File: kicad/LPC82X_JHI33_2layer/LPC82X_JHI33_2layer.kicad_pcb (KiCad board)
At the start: 2 copper layers, 26 x 23.5 mm, 27 parts, among them J1 Conn_02x09_Odd_Even, J2 Conn_02x09_Odd_Even, J3 JTAG_2X05, U1 LPC824M201JHI33, Y1 12MHz

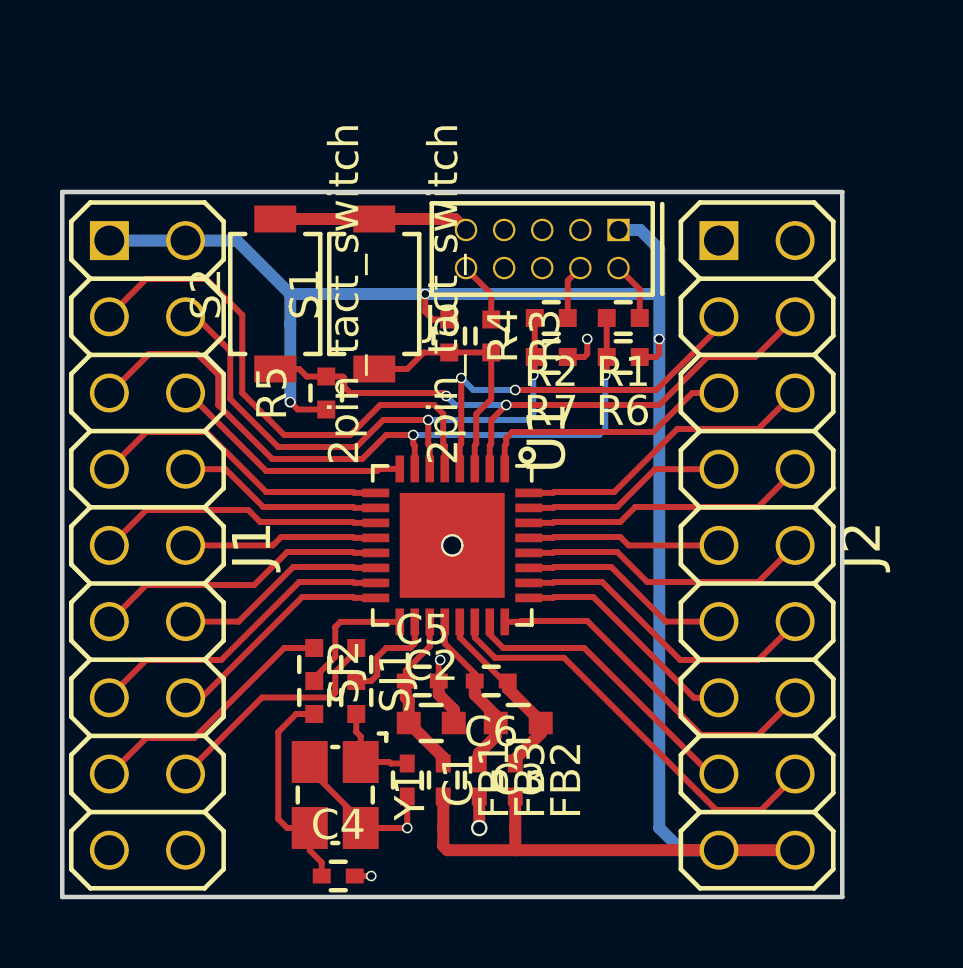
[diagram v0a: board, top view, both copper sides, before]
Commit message: added bulk decoupling 0805 increased clearance of ground plane
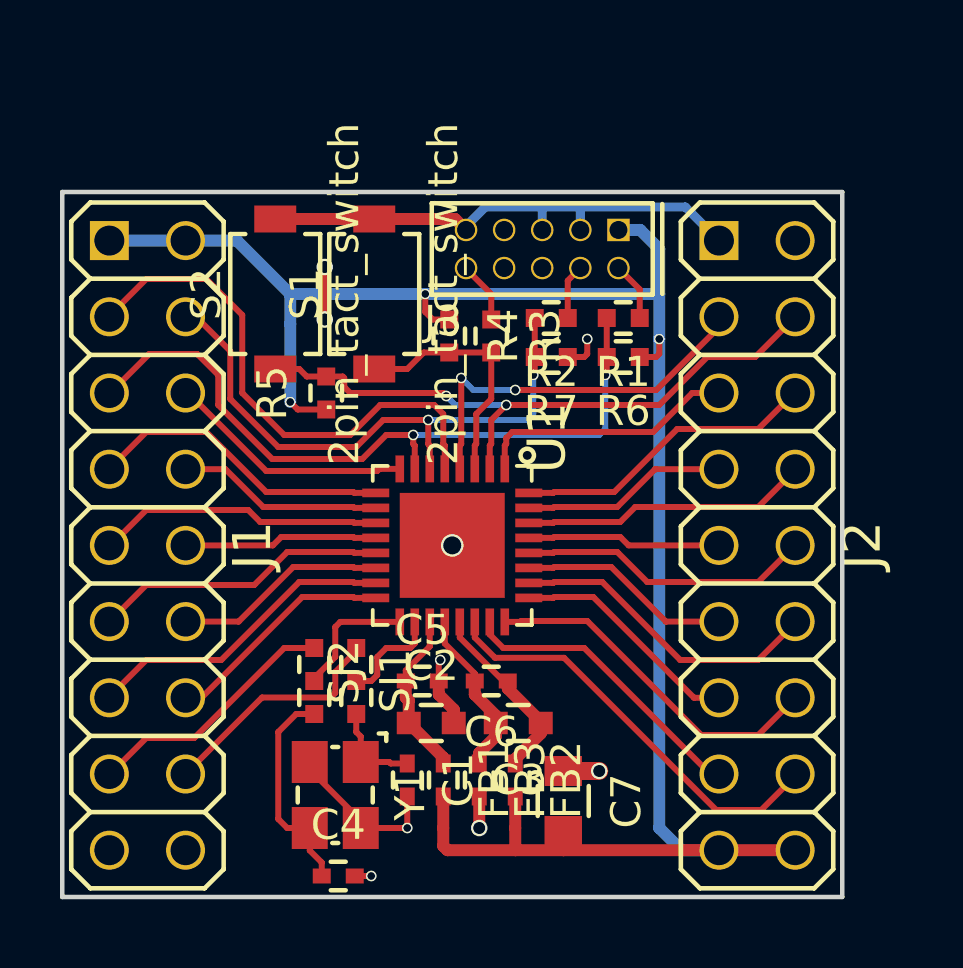
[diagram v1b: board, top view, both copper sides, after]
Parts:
- added C7: 10u, SquantorRcl:C_0805, F.Cu at (92.6, 115.2)
- FB1, FB2, FB3: value Ferrite_Bead_Small -> FB
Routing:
- net VSS: track 17.1 -> 31.1 mm, vias 6 -> 9
- net VDD: track 65.1 -> 65.8 mm
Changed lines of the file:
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@@
     (thickness 1.6)
     (drawings 4)
-    (tracks 351)
+    (tracks 368)
     (zones 0)
-    (modules 27)
+    (modules 28)
     (nets 42)
   )
@@
   )
   (setup
-    (last_trace_width 0.2)
+    (last_trace_width 0.3)
     (user_trace_width 0.127)
     (user_trace_width 0.2)
@@
     (user_trace_width 2)
     (trace_clearance 0.127)
-    (zone_clearance 0.2)
+    (zone_clearance 0.3)
     (zone_45_only no)
     (trace_min 0.127)
@@
       (effects (font (size 1 1) (thickness 0.15)))
     )
-    (fp_text value Ferrite_Bead_Small (at 0 1.7) (layer F.Fab)
+    (fp_text value FB (at 0 1.7) (layer F.Fab)
       (effects (font (size 1 1) (thickness 0.15)))
     )
@@
       (effects (font (size 1 1) (thickness 0.15)))
     )
-    (fp_text value Ferrite_Bead_Small (at 0 1.7 270) (layer F.Fab)
+    (fp_text value FB (at 0 1.7 270) (layer F.Fab)
       (effects (font (size 1 1) (thickness 0.15)))
     )
@@
       (effects (font (size 1 1) (thickness 0.15)))
     )
-    (fp_text value Ferrite_Bead_Small (at 0 1.7 270) (layer F.Fab)
+    (fp_text value FB (at 0 1.7 270) (layer F.Fab)
       (effects (font (size 1 1) (thickness 0.15)))
     )
@@
     )
   )
+  (module SquantorRcl:C_0805 (layer F.Cu)
+    (at 92.6 115.2 270)
+    (descr "Capacitor SMD 0805, reflow soldering, AVX (see smccp.pdf)")
+    (tags "capacitor 0805")
+    (attr smd)
+    (fp_text reference C7 (at 0 -2.1 270) (layer F.SilkS)
+      (effects (font (size 1 1) (thickness 0.15)))
+    )
+    (fp_text value 10u (at 0 2.1 270) (layer F.Fab)
+      (effects (font (size 1 1) (thickness 0.15)))
+    )
+    (fp_line (start -1 0.625) (end -1 -0.625) (layer F.Fab) (width 0.15))
+    (fp_line (start 1 0.625) (end -1 0.625) (layer F.Fab) (width 0.15))
+    (fp_line (start 1 -0.625) (end 1 0.625) (layer F.Fab) (width 0.15))
+    (fp_line (start -1 -0.625) (end 1 -0.625) (layer F.Fab) (width 0.15))
+    (fp_line (start -1.8 -1) (end 1.8 -1) (layer F.CrtYd) (width 0.05))
+    (fp_line (start -1.8 1) (end 1.8 1) (layer F.CrtYd) (width 0.05))
+    (fp_line (start -1.8 -1) (end -1.8 1) (layer F.CrtYd) (width 0.05))
+    (fp_line (start 1.8 -1) (end 1.8 1) (layer F.CrtYd) (width 0.05))
+    (fp_line (start 0.5 -0.85) (end -0.5 -0.85) (layer F.SilkS) (width 0.15))
+    (fp_line (start -0.5 0.85) (end 0.5 0.85) (layer F.SilkS) (width 0.15))
+    (pad 1 smd rect (at -1 0 270) (size 1 1.25) (layers F.Cu F.Paste F.Mask)
+      (net 2 VSS))
+    (pad 2 smd rect (at 1 0 270) (size 1 1.25) (layers F.Cu F.Paste F.Mask)
+      (net 7 VDD))
+    (model Capacitors_SMD.3dshapes/C_0805.wrl
+      (at (xyz 0 0 0))
+      (scale (xyz 1 1 1))
+      (rotate (xyz 0 0 0))
+    )
+  )
   (gr_line (start 75.9 118.4) (end 75.9 94.9) (layer Edge.Cuts) (width 0.15))
   (gr_line (start 101.9 118.4) (end 75.9 118.4) (layer Edge.Cuts) (width 0.15))
   (gr_line (start 101.9 94.9) (end 101.9 118.4) (layer Edge.Cuts) (width 0.15))
   (gr_line (start 75.9 94.9) (end 101.9 94.9) (layer Edge.Cuts) (width 0.15))
+  (via (at 84.65 99.15) (size 0.55) (drill 0.4) (layers F.Cu B.Cu) (net 2))
+  (segment (start 84.65 99.15) (end 84.65 97.4) (width 0.3) (layer F.Cu) (net 2))
+  (via (at 84.65 97.4) (size 0.55) (drill 0.4) (layers F.Cu B.Cu) (net 2))
   (segment (start 85.7 112.3) (end 85.7 112.9) (width 0.2) (layer F.Cu) (net 1))
   (segment (start 85.85 113.05) (end 85.85 113.9) (width 0.2) (layer F.Cu) (net 1))
@@
   (segment (start 88.995 95.8) (end 89.36 96.165) (width 0.4) (layer F.Cu) (net 2))
   (segment (start 86.3 95.8) (end 88.995 95.8) (width 0.4) (layer F.Cu) (net 2))
+  (segment (start 92.6 114.2) (end 93.8 114.2) (width 0.6) (layer F.Cu) (net 2))
+  (via (at 93.8 114.2) (size 0.55) (drill 0.4) (layers F.Cu B.Cu) (net 2))
+  (segment (start 89.36 96.165) (end 89.36 96.04) (width 0.3) (layer F.Cu) (net 2))
+  (segment (start 89.36 96.165) (end 89.36 96.04) (width 0.3) (layer B.Cu) (net 2))
+  (segment (start 89.36 96.04) (end 90 95.4) (width 0.3) (layer B.Cu) (net 2))
+  (segment (start 91.9 96.165) (end 91.9 95.4) (width 0.3) (layer B.Cu) (net 2))
+  (segment (start 90 95.4) (end 91.9 95.4) (width 0.3) (layer B.Cu) (net 2))
+  (segment (start 96.67 95.4) (end 97.79 96.52) (width 0.3) (layer B.Cu) (net 2))
+  (segment (start 93.17 95.48) (end 93.25 95.4) (width 0.3) (layer B.Cu) (net 2))
+  (segment (start 93.17 96.165) (end 93.17 95.48) (width 0.3) (layer B.Cu) (net 2))
+  (segment (start 91.9 95.4) (end 93.25 95.4) (width 0.3) (layer B.Cu) (net 2))
+  (segment (start 93.25 95.4) (end 96.67 95.4) (width 0.3) (layer B.Cu) (net 2))
   (segment (start 87.35 111.2) (end 87.35 110.85) (width 0.2) (layer F.Cu) (net 3))
   (segment (start 88.15 110.05) (end 88.15 109.23) (width 0.2) (layer F.Cu) (net 3))
@@
   (segment (start 88.74 116.84) (end 88.6 116.7) (width 0.4) (layer F.Cu) (net 7))
   (segment (start 91 116.1) (end 91 116.84) (width 0.4) (layer F.Cu) (net 7))
-  (segment (start 97.79 116.84) (end 91 116.84) (width 0.4) (layer F.Cu) (net 7))
   (segment (start 91 116.84) (end 88.74 116.84) (width 0.4) (layer F.Cu) (net 7))
   (segment (start 77.47 96.52) (end 80.01 96.52) (width 0.4) (layer B.Cu) (net 7))
@@
   (segment (start 83.5 98.3) (end 88 98.3) (width 0.4) (layer B.Cu) (net 7))
   (segment (start 88 98.3) (end 95.8 98.3) (width 0.4) (layer B.Cu) (net 7))
+  (segment (start 92.6 116.2) (end 92.6 116.84) (width 0.4) (layer F.Cu) (net 7))
+  (segment (start 97.79 116.84) (end 92.6 116.84) (width 0.4) (layer F.Cu) (net 7))
+  (segment (start 92.6 116.84) (end 91 116.84) (width 0.4) (layer F.Cu) (net 7))
   (segment (start 77.47 99.06) (end 77.47 99.03) (width 0.2) (layer B.Cu) (net 8))
   (segment (start 88.65 103.35) (end 88.65 104.13) (width 0.2) (layer F.Cu) (net 8))
@@
   (segment (start 85.17 109.23) (end 85 109.4) (width 0.2) (layer F.Cu) (net 41))
   (zone (net 2) (net_name VSS) (layer B.Cu) (hatch edge 0.508)
-    (connect_pads (clearance 0.2))
-    (min_thickness 0.254)
+    (connect_pads (clearance 0.3))
+    (min_thickness 0.4)
     (fill yes (arc_segments 16) (thermal_gap 0.508) (thermal_bridge_width 0.508))
     (polygon

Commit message: silk screen updates
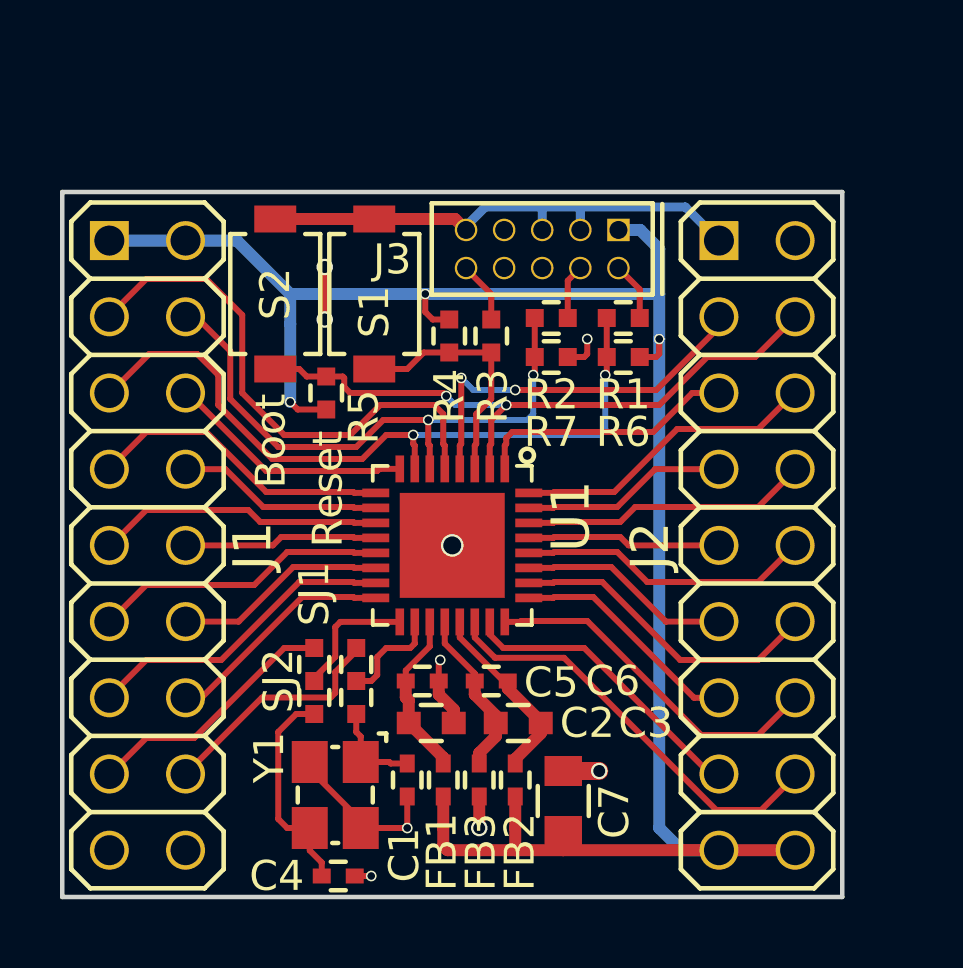
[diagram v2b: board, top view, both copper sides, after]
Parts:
- S1: value 2pin_tact_switch -> Reset
- S2: value 2pin_tact_switch -> Boot
- moved N2 9.19 mm to (84.2, 110.5)
- moved N1 9.12 mm to (85.0, 106.8)

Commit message: updated versionnumber
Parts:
- N2: value 20181026 -> 20181028
- moved N2 8.81 mm to (92.6, 108.0), turned to 270 degrees
- moved N1 3.70 mm to (88.7, 106.7), turned to 270 degrees
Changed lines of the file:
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@@
   )
   (module Symbols:OSHW-Symbol_6.7x6mm_SilkScreen (layer B.Cu)
-    (at 85 106.8 180)
+    (at 88.7 106.7 270)
     (descr "Open Source Hardware Symbol")
     (tags "Logo Symbol OSHW")
     (attr virtual)
-    (fp_text reference N1 (at 0 0 180) (layer B.SilkS) hide
+    (fp_text reference N1 (at 0 0 270) (layer B.SilkS) hide
       (effects (font (size 1 1) (thickness 0.15)) (justify mirror))
     )
-    (fp_text value OHWLOGO (at 0.75 0 180) (layer B.Fab) hide
+    (fp_text value OHWLOGO (at 0.75 0 270) (layer B.Fab) hide
       (effects (font (size 1 1) (thickness 0.15)) (justify mirror))
     )
@@
   )
   (module SquantorLabels:Label_version (layer B.Cu)
-    (at 84.15 110.45 180)
-    (fp_text reference N2 (at 0 -1.4 180) (layer B.Fab) hide
+    (at 92.6 107.95 270)
+    (fp_text reference N2 (at 0 -1.4 270) (layer B.Fab) hide
       (effects (font (size 1 1) (thickness 0.15)) (justify mirror))
     )
-    (fp_text value 20181026 (at -0.4 0.137362 180) (layer B.SilkS)
+    (fp_text value 20181028 (at -0.4 0.137362 270) (layer B.SilkS)
       (effects (font (size 1 1) (thickness 0.15)) (justify mirror))
     )
-    (fp_text user V: (at -4.9 0.1 180) (layer B.SilkS)
+    (fp_text user V: (at -4.9 0.1 270) (layer B.SilkS)
       (effects (font (size 1 1) (thickness 0.15)) (justify mirror))
     )

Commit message: updated schematic bits updated board and rerouted with some deletions, lets see if we can shrink the board a bit
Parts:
- removed R5: 47K, SquantorRcl:R_0402_hand
- removed S1: Reset, SquantorButtons:TD-85XU
- removed S2: Boot, SquantorButtons:TD-85XU
- removed SJ1, SJ2: SolderJumper_3way_1conn, SquantorSpecial:solder_jumper_3way_12conn
- N2: value 20181028 -> 20181029
- R4: value 47K -> 100K
- moved C1 5.10 mm to (84.9, 110.0), turned to 180 degrees
- moved C4 2.36 mm to (84.9, 115.3)
- moved Y1 2.30 mm to (84.9, 112.7)
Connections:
- C1 pad 1: /XTALIN -> /PIO0_9
- C4 pad 1: /XTALOUT -> /PIO0_8
- U1 pad 17: /PIO0_9-XTALOUT -> /PIO0_9
- U1 pad 18: /PIO0_8-XTALIN -> /PIO0_8
- Y1 pad 1: /XTALIN -> /PIO0_9
- Y1 pad 3: /XTALOUT -> /PIO0_8
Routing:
- net /PIO0_8: track 7.90 -> 17.1 mm
- net /PIO0_12: track 21.6 -> 13.2 mm, vias 2 -> 0
- net /XTALOUT: track 7.29 -> 0.00 mm
- net VSS: track 31.1 -> 24.7 mm, vias 9 -> 8
- net /PIO0_9: track 8.57 -> 14.3 mm
- net VDD: track 65.8 -> 60.8 mm, vias 3 -> 2
- net /PIO0_9-XTALOUT: track 4.31 -> 0.00 mm
- net /PIO0_8-XTALIN: track 3.54 -> 0.00 mm
- net /XTALIN: track 3.23 -> 0.00 mm
- net /RESET: track 8.24 -> 5.51 mm
- net /PIO0_4: track 13.0 -> 12.2 mm

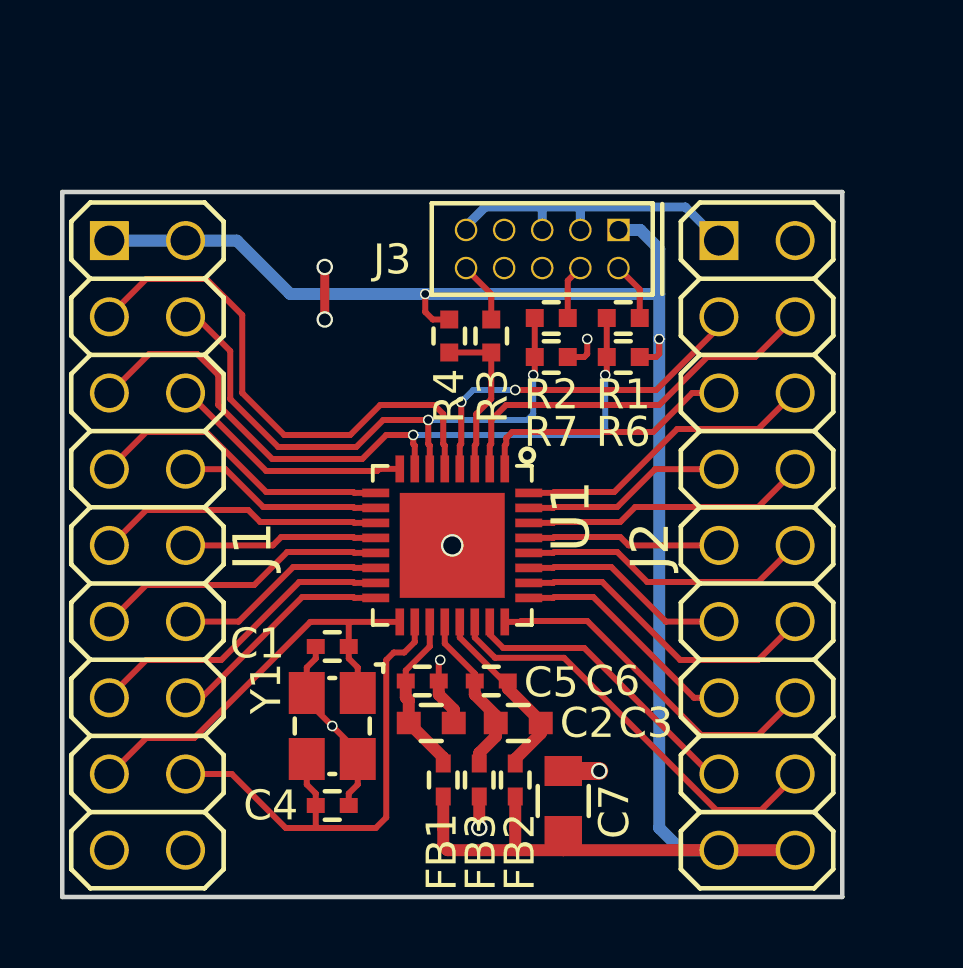
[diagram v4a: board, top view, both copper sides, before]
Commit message: reduced PCB size, rerouting large parts of it
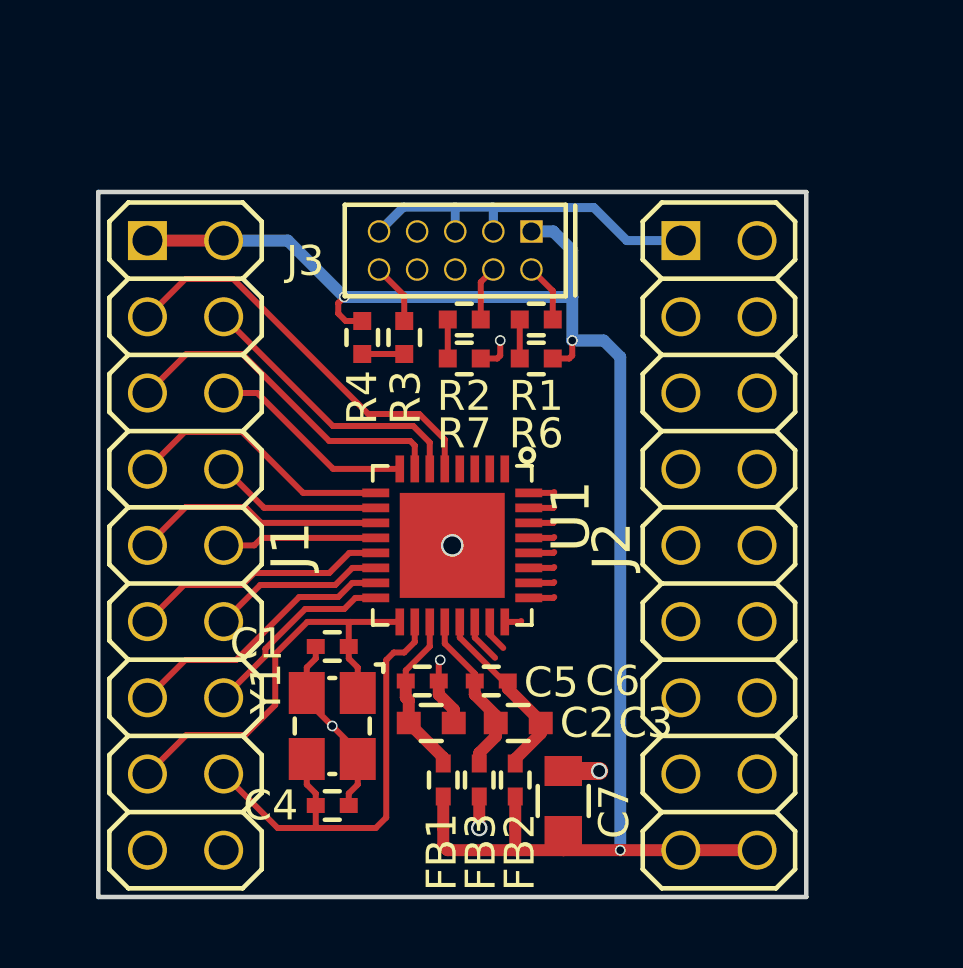
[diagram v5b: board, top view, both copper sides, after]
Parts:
- moved J3 2.90 mm to (89.0, 96.8)
- moved R2 2.90 mm to (89.3, 99.2)
- moved R3 2.90 mm to (87.3, 99.8)
- moved R7 2.90 mm to (89.3, 100.5)
- moved R1 2.90 mm to (91.7, 99.2)
- moved R4 2.90 mm to (85.9, 99.8)
- moved R6 2.90 mm to (91.7, 100.5)
- moved J1 1.27 mm to (80.0, 106.7)
- moved J2 1.27 mm to (97.8, 106.7)
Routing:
- net /PIO0_12: track 13.2 -> 0.00 mm
- net /PIO0_7: track 14.1 -> 1.48 mm
- net /PIO0_4: track 12.2 -> 0.00 mm, vias 2 -> 0
- net /PIO0_2: track 24.4 -> 12.8 mm, vias 2 -> 0
- net /PIO0_0: track 11.8 -> 0.56 mm
- net /PIO0_23: track 10.5 -> 0.86 mm
- net /PIO0_17: track 10.3 -> 0.86 mm
- net /PIO0_21: track 9.81 -> 0.86 mm
- net /PIO0_6: track 9.99 -> 1.06 mm
- net /PIO0_3: track 19.7 -> 10.8 mm, vias 2 -> 0
- net /PIO0_19: track 9.64 -> 0.86 mm
- net /PIO0_13: track 8.76 -> 0.00 mm
- net /PIO0_14: track 7.74 -> 0.86 mm
- net /PIO0_22: track 7.11 -> 0.86 mm
- net /PIO0_18: track 6.87 -> 0.86 mm
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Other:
- board size 26 x 23.5 mm -> 23.6 x 23.5 mm
